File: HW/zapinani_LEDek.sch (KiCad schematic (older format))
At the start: 0 parts

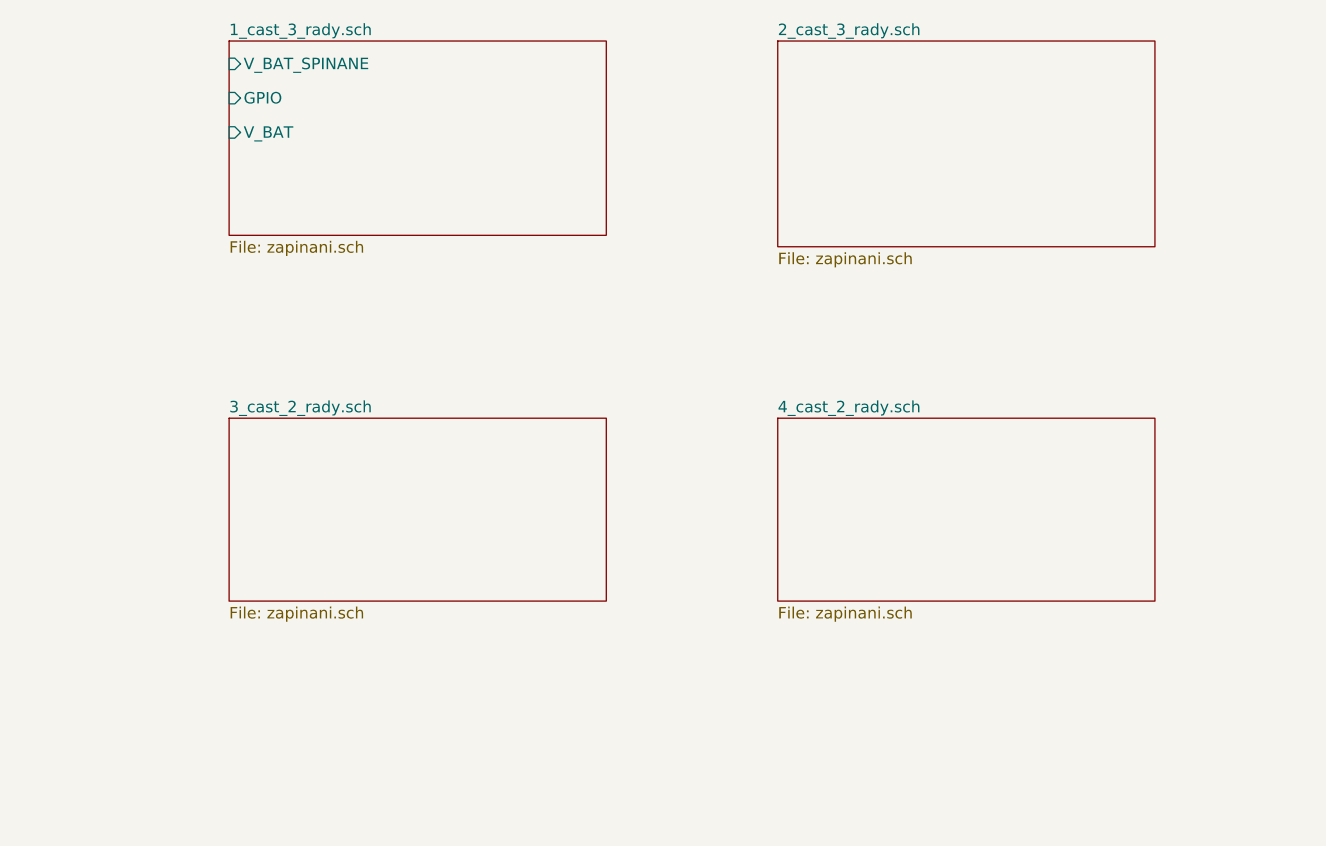
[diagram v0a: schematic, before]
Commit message: change structure of LEDs, add switching power supply of LEDs in parts
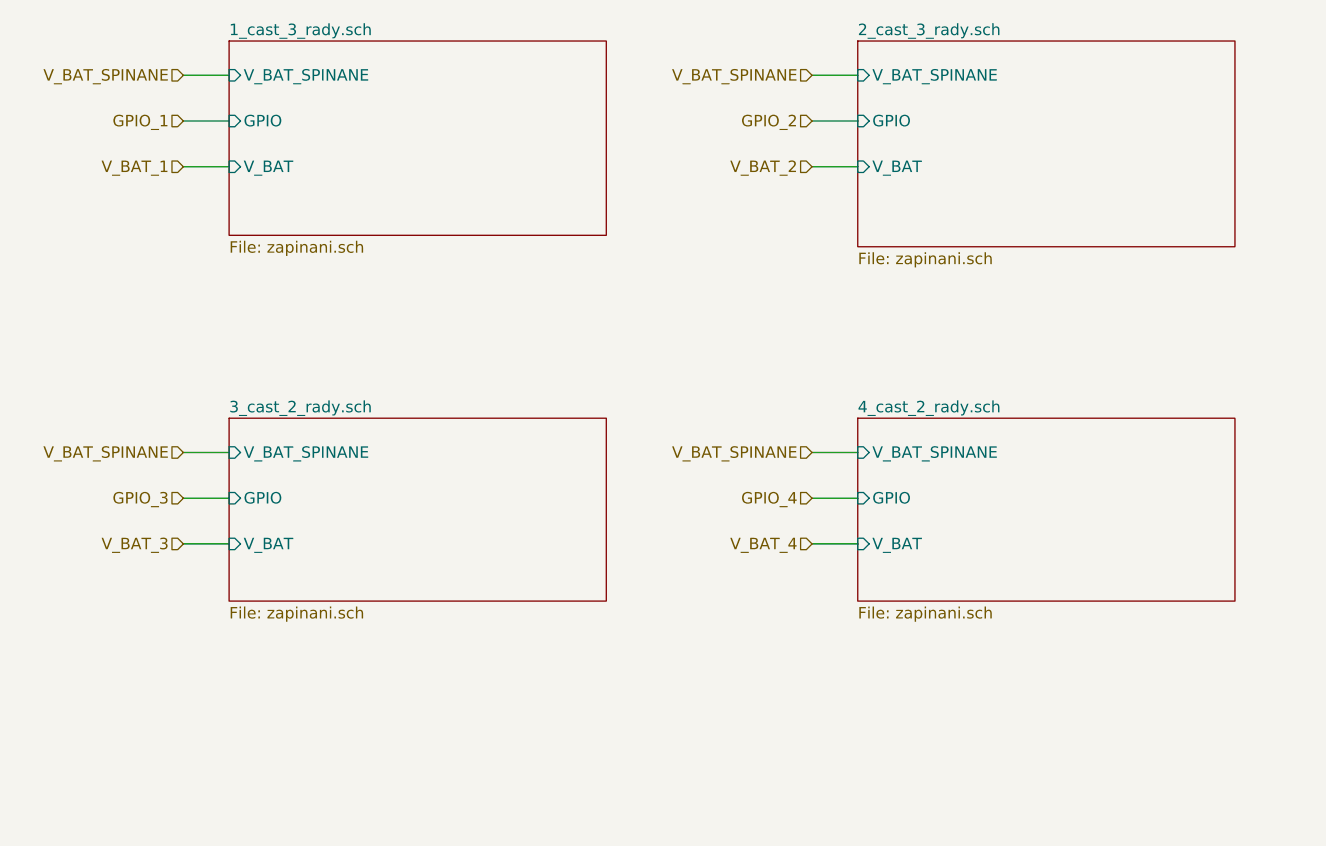
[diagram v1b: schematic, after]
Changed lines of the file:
@@
 $Descr A4 11693 8268
 encoding utf-8
-Sheet 18 22
+Sheet 18 42
 Title ""
 Date ""
@@
 F0 "1_cast_3_rady.sch" 50
 F1 "zapinani.sch" 50
-F2 "V_BAT_SPINANE" I L 1900 1150 50
-F3 "GPIO" I L 1900 1300 50
-F4 "V_BAT" I L 1900 1450 50
+F2 "V_BAT_SPINANE" I L 1900 1200 50
+F3 "GPIO" I L 1900 1400 50
+F4 "V_BAT" I L 1900 1600 50
 $EndSheet
 $Sheet
-S 4300 1050 1650 900
+S 4650 1050 1650 900
 U 5F7BCBA6
 F0 "2_cast_3_rady.sch" 50
 F1 "zapinani.sch" 50
+F2 "V_BAT_SPINANE" I L 4650 1200 50
+F3 "GPIO" I L 4650 1400 50
+F4 "V_BAT" I L 4650 1600 50
 $EndSheet
 $Sheet
@@
 F0 "3_cast_2_rady.sch" 50
 F1 "zapinani.sch" 50
+F2 "V_BAT_SPINANE" I L 1900 2850 50
+F3 "GPIO" I L 1900 3050 50
+F4 "V_BAT" I L 1900 3250 50
 $EndSheet
 $Sheet
-S 4300 2700 1650 800
+S 4650 2700 1650 800
 U 5F7BCC69
 F0 "4_cast_2_rady.sch" 50
 F1 "zapinani.sch" 50
+F2 "V_BAT_SPINANE" I L 4650 2850 50
+F3 "GPIO" I L 4650 3050 50
+F4 "V_BAT" I L 4650 3250 50
 $EndSheet
+Text HLabel 1700 1200 0    50   Input ~ 0
+V_BAT_SPINANE
+Text HLabel 4450 1200 0    50   Input ~ 0
+V_BAT_SPINANE
+Text HLabel 4450 2850 0    50   Input ~ 0
+V_BAT_SPINANE
+Text HLabel 1700 2850 0    50   Input ~ 0
+V_BAT_SPINANE
+Text HLabel 1700 1600 0    50   Input ~ 0
+V_BAT_1
+Text HLabel 4450 1600 0    50   Input ~ 0
+V_BAT_2
+Text HLabel 4450 3250 0    50   Input ~ 0
+V_BAT_4
+Text HLabel 1700 3250 0    50   Input ~ 0
+V_BAT_3
+Text HLabel 1700 1400 0    50   Input ~ 0
+GPIO_1
+Text HLabel 4450 1400 0    50   Input ~ 0
+GPIO_2
+Text HLabel 1700 3050 0    50   Input ~ 0
+GPIO_3
+Text HLabel 4450 3050 0    50   Input ~ 0
+GPIO_4
+Wire Wire Line
+	1700 1200 1900 1200
+Wire Wire Line
+	1900 1400 1700 1400
+Wire Wire Line
+	1700 1600 1900 1600
+Wire Wire Line
+	4450 1200 4650 1200
+Wire Wire Line
+	4650 1400 4450 1400
+Wire Wire Line
+	4450 1600 4650 1600
+Wire Wire Line
+	4650 2850 4450 2850
+Wire Wire Line
+	4450 3050 4650 3050
+Wire Wire Line
+	4650 3250 4450 3250
+Wire Wire Line
+	1700 2850 1900 2850
+Wire Wire Line
+	1900 3050 1700 3050
+Wire Wire Line
+	1700 3250 1900 3250
 $EndSCHEMATC

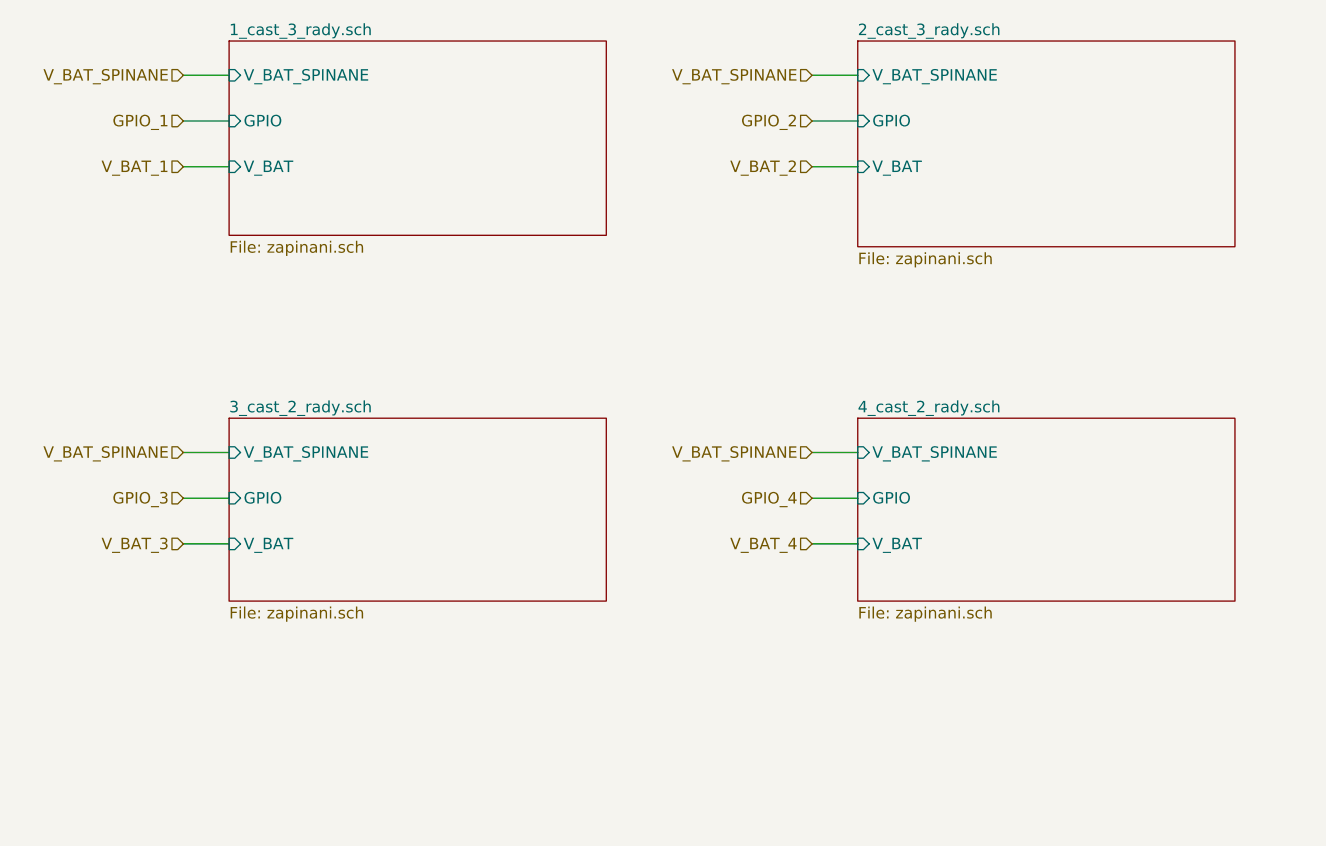
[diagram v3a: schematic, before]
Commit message: make smaller test version, start routing
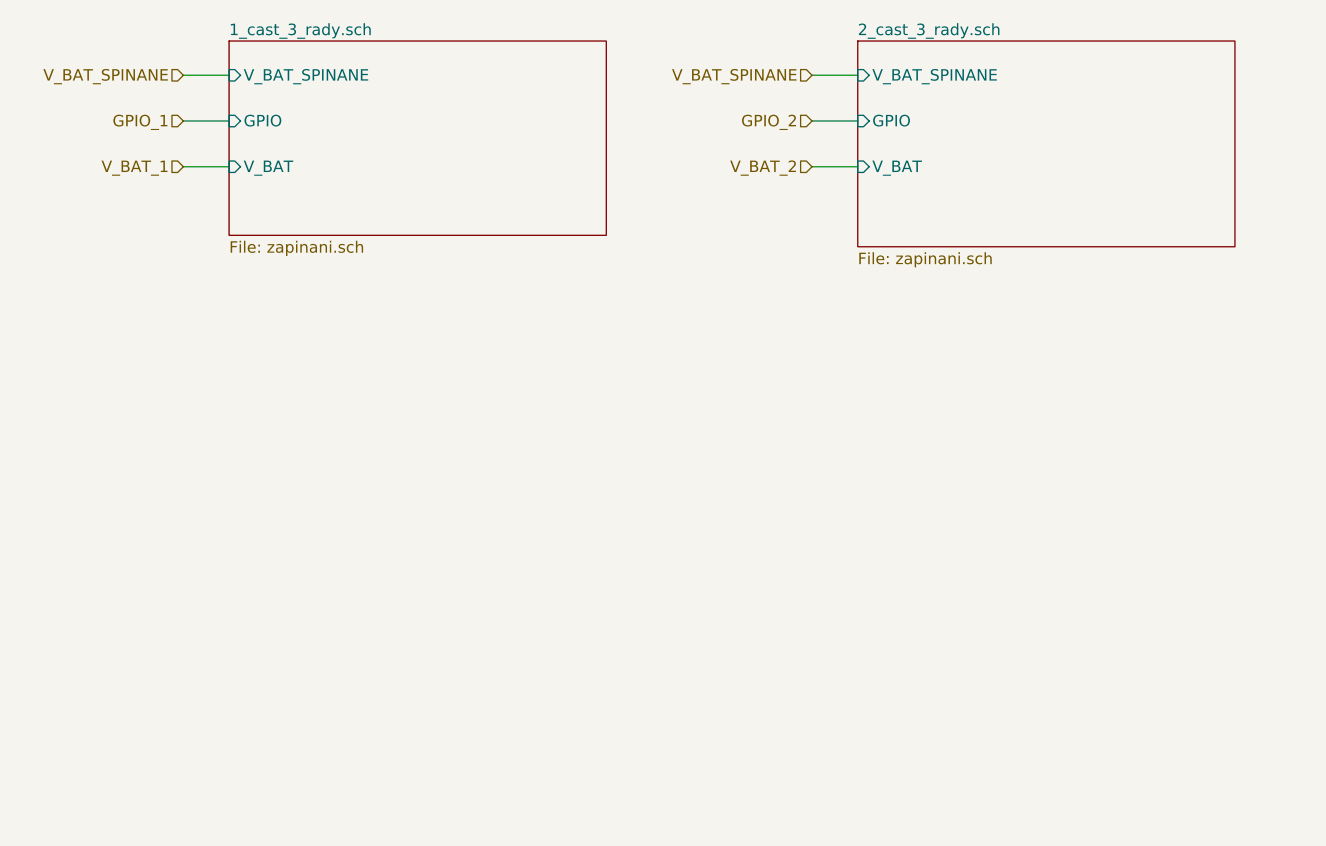
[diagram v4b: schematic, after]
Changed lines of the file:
@@
 $Descr A4 11693 8268
 encoding utf-8
-Sheet 16 44
+Sheet 16 34
 Title ""
 Date ""
@@
 F4 "V_BAT" I L 4650 1600 50
 $EndSheet
-$Sheet
-S 1900 2700 1650 800
-U 5F7BCC0A
-F0 "3_cast_2_rady.sch" 50
-F1 "zapinani.sch" 50
-F2 "V_BAT_SPINANE" I L 1900 2850 50
-F3 "GPIO" I L 1900 3050 50
-F4 "V_BAT" I L 1900 3250 50
-$EndSheet
-$Sheet
-S 4650 2700 1650 800
-U 5F7BCC69
-F0 "4_cast_2_rady.sch" 50
-F1 "zapinani.sch" 50
-F2 "V_BAT_SPINANE" I L 4650 2850 50
-F3 "GPIO" I L 4650 3050 50
-F4 "V_BAT" I L 4650 3250 50
-$EndSheet
 Text HLabel 1700 1200 0    50   Input ~ 0
 V_BAT_SPINANE
 Text HLabel 4450 1200 0    50   Input ~ 0
-V_BAT_SPINANE
-Text HLabel 4450 2850 0    50   Input ~ 0
-V_BAT_SPINANE
-Text HLabel 1700 2850 0    50   Input ~ 0
 V_BAT_SPINANE
 Text HLabel 1700 1600 0    50   Input ~ 0
@@
 Text HLabel 4450 1600 0    50   Input ~ 0
 V_BAT_2
-Text HLabel 4450 3250 0    50   Input ~ 0
-V_BAT_4
-Text HLabel 1700 3250 0    50   Input ~ 0
-V_BAT_3
 Text HLabel 1700 1400 0    50   Input ~ 0
 GPIO_1
 Text HLabel 4450 1400 0    50   Input ~ 0
 GPIO_2
-Text HLabel 1700 3050 0    50   Input ~ 0
-GPIO_3
-Text HLabel 4450 3050 0    50   Input ~ 0
-GPIO_4
 Wire Wire Line
 	1700 1200 1900 1200
@@
 Wire Wire Line
 	4450 1600 4650 1600
-Wire Wire Line
-	4650 2850 4450 2850
-Wire Wire Line
-	4450 3050 4650 3050
-Wire Wire Line
-	4650 3250 4450 3250
-Wire Wire Line
-	1700 2850 1900 2850
-Wire Wire Line
-	1900 3050 1700 3050
-Wire Wire Line
-	1700 3250 1900 3250
 $EndSCHEMATC

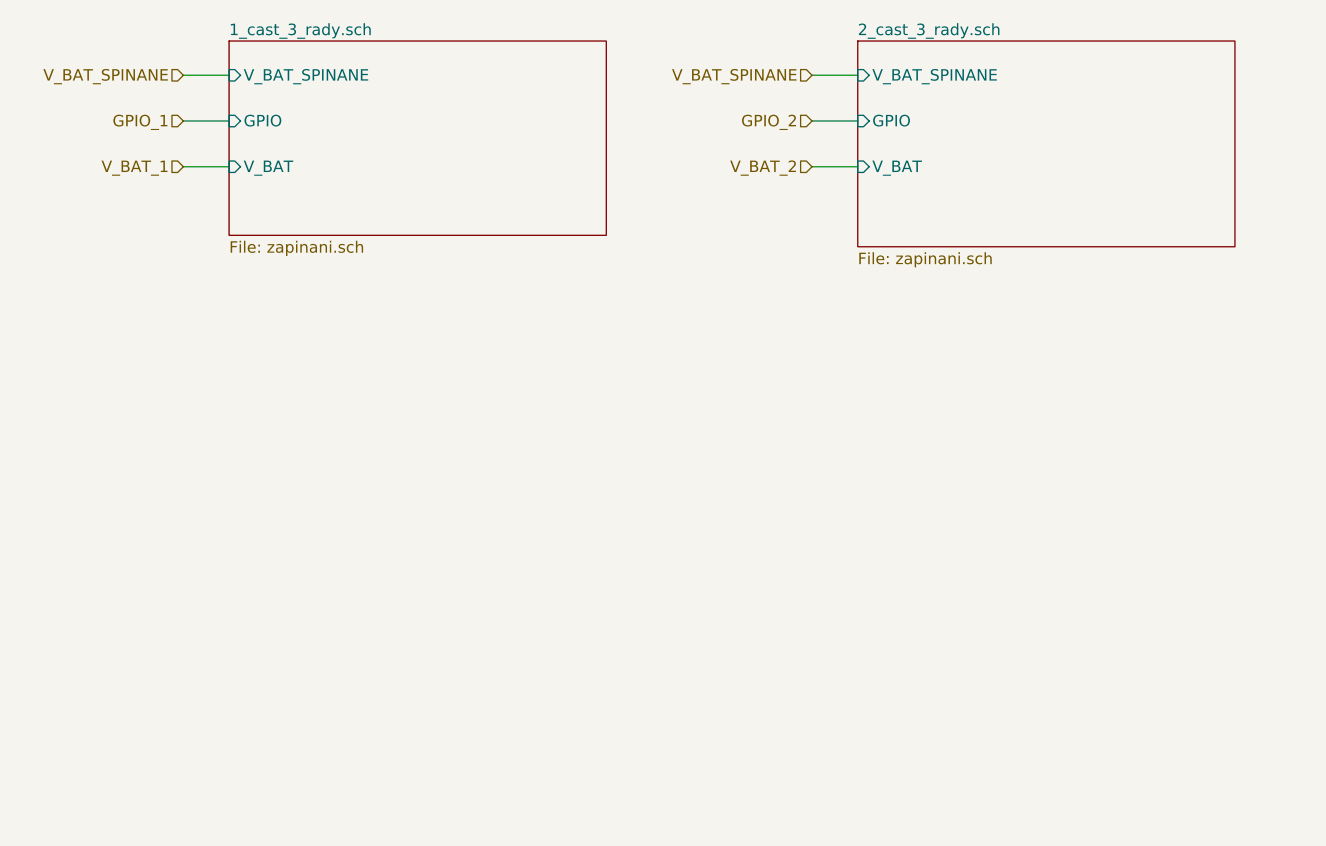
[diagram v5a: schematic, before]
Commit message: change structure of buttons, switching power
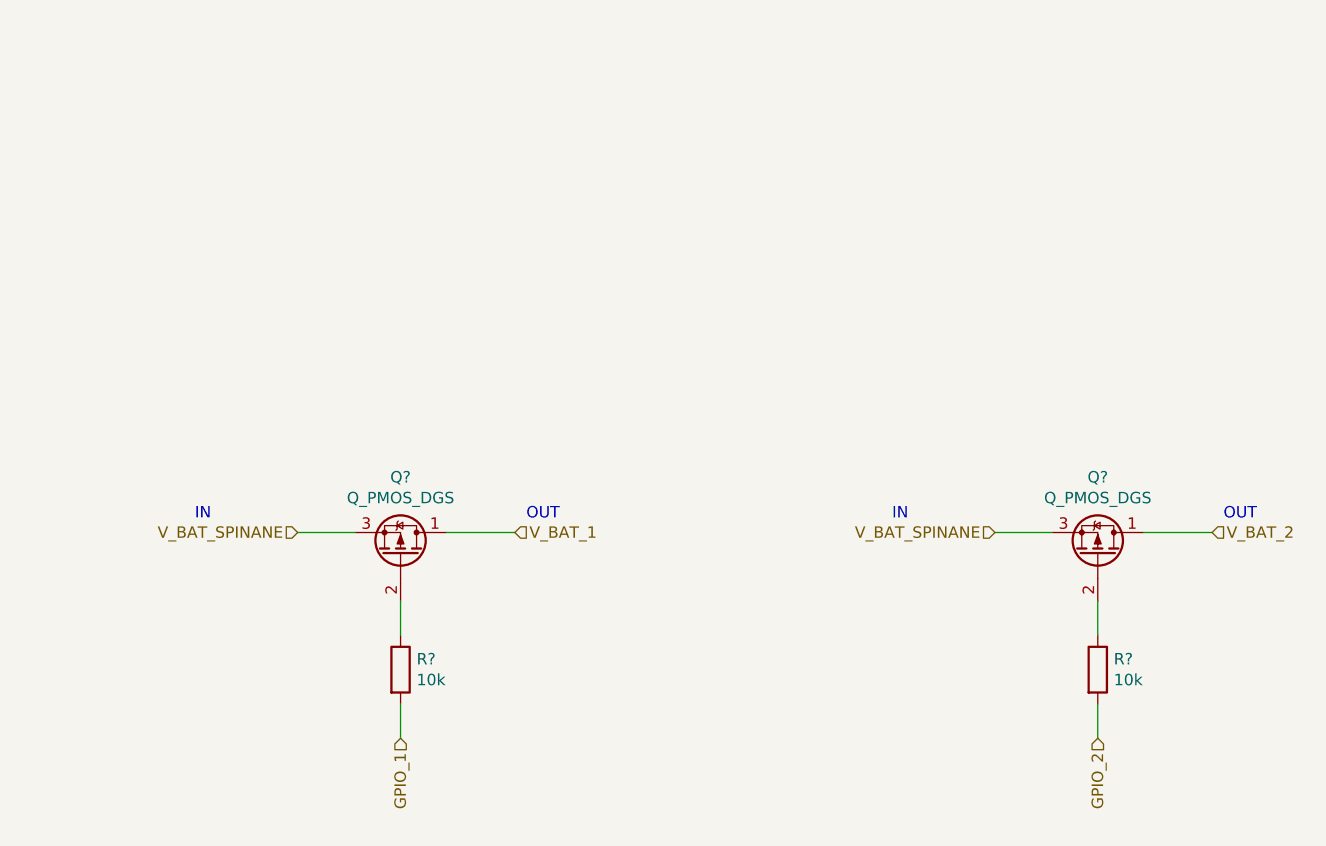
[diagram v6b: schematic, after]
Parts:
- added Q? (x2): Q_PMOS_DGS, Package_TO_SOT_SMD:SOT-23, symbol Device:Q_PMOS_DGS
- added R? (x2): 10k, Resistor_SMD:R_0402_1005Metric, symbol Device:R
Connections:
- net GPIO_1: now also R?.2
- net GPIO_2: now also R?.2
- net V_BAT_1: now also Q?.1 (D)
- net V_BAT_2: now also Q?.1 (D)
- net V_BAT_SPINANE: now also Q?.3 (S), Q?.3 (S)
- new net: Q?.2 (G), R?.1 (x2)
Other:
- note added: "IN\n"
- note added: "OUT\n"
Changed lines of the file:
@@
 $Descr A4 11693 8268
 encoding utf-8
-Sheet 32 34
+Sheet 21 21
 Title ""
 Date ""
@@
 Comment4 ""
 $EndDescr
-$Sheet
-S 1900 1050 1650 850
-U 5F7BCB45
-F0 "1_cast_3_rady.sch" 50
-F1 "zapinani.sch" 50
-F2 "V_BAT_SPINANE" I L 1900 1200 50
-F3 "GPIO" I L 1900 1400 50
-F4 "V_BAT" I L 1900 1600 50
-$EndSheet
-$Sheet
-S 4650 1050 1650 900
-U 5F7BCBA6
-F0 "2_cast_3_rady.sch" 50
-F1 "zapinani.sch" 50
-F2 "V_BAT_SPINANE" I L 4650 1200 50
-F3 "GPIO" I L 4650 1400 50
-F4 "V_BAT" I L 4650 1600 50
-$EndSheet
-Text HLabel 1700 1200 0    50   Input ~ 0
+Text HLabel 3150 3200 2    50   Input ~ 0
+V_BAT_1
+Text HLabel 2650 4100 3    50   Input ~ 0
+GPIO_1
+$Comp
+L Device:Q_PMOS_DGS Q?
+U 1 1 5F8EC64F
+P 2650 3300
+AR Path="/5F8EC64F" Ref="Q?"  Part="1"
+AR Path="/5F7BA54B/5F8EC64F" Ref="Q?"  Part="1"
+AR Path="/5F7BA54B/5F7BCB45/5F8EC64F" Ref="Q?"  Part="1"
+AR Path="/5F7BA54B/5F7BCBA6/5F8EC64F" Ref="Q?"  Part="1"
+AR Path="/5F7BA54B/5F7BCC0A/5F8EC64F" Ref="Q?"  Part="1"
+AR Path="/5F7BA54B/5F7BCC69/5F8EC64F" Ref="Q?"  Part="1"
+F 0 "Q?" V 2992 3300 50  0000 C CNN
+F 1 "Q_PMOS_DGS" V 2901 3300 50  0000 C CNN
+F 2 "Package_TO_SOT_SMD:SOT-23" H 2850 3400 50  0001 C CNN
+F 3 "~" H 2650 3300 50  0001 C CNN
+F 4 "C15127" H 2650 3300 50  0001 C CNN "LCSC"
+F 5 "0;0;180" H 2650 3300 50  0001 C CNN "JLCPCB_CORRECTION"
+	1    2650 3300
+	0    1    -1   0
+$EndComp
+$Comp
+L Device:R R?
+U 1 1 5F8EC656
+P 2650 3800
+AR Path="/5F8EC656" Ref="R?"  Part="1"
+AR Path="/5F7BA54B/5F8EC656" Ref="R?"  Part="1"
+AR Path="/5F7BA54B/5F7BCB45/5F8EC656" Ref="R?"  Part="1"
+AR Path="/5F7BA54B/5F7BCBA6/5F8EC656" Ref="R?"  Part="1"
+AR Path="/5F7BA54B/5F7BCC0A/5F8EC656" Ref="R?"  Part="1"
+AR Path="/5F7BA54B/5F7BCC69/5F8EC656" Ref="R?"  Part="1"
+F 0 "R?" H 2720 3846 50  0000 L CNN
+F 1 "10k" H 2720 3755 50  0000 L CNN
+F 2 "Resistor_SMD:R_0402_1005Metric" V 2580 3800 50  0001 C CNN
+F 3 "~" H 2650 3800 50  0001 C CNN
+F 4 "C25744" H 2650 3800 50  0001 C CNN "LCSC"
+	1    2650 3800
+	1    0    0    -1
+$EndComp
+Wire Wire Line
+	2200 3200 2450 3200
+Wire Wire Line
+	2850 3200 3150 3200
+Wire Wire Line
+	2650 3500 2650 3650
+Wire Wire Line
+	2650 3950 2650 4100
+Text HLabel 2200 3200 0    50   Input ~ 0
 V_BAT_SPINANE
-Text HLabel 4450 1200 0    50   Input ~ 0
+Text Notes 1750 3150 0    50   ~ 0
+IN\n
+Text Notes 3200 3150 0    50   ~ 0
+OUT\n
+Text HLabel 6200 3200 2    50   Input ~ 0
+V_BAT_2
+Text HLabel 5700 4100 3    50   Input ~ 0
+GPIO_2
+$Comp
+L Device:Q_PMOS_DGS Q?
+U 1 1 5F8ECA64
+P 5700 3300
+AR Path="/5F8ECA64" Ref="Q?"  Part="1"
+AR Path="/5F7BA54B/5F8ECA64" Ref="Q?"  Part="1"
+AR Path="/5F7BA54B/5F7BCB45/5F8ECA64" Ref="Q?"  Part="1"
+AR Path="/5F7BA54B/5F7BCBA6/5F8ECA64" Ref="Q?"  Part="1"
+AR Path="/5F7BA54B/5F7BCC0A/5F8ECA64" Ref="Q?"  Part="1"
+AR Path="/5F7BA54B/5F7BCC69/5F8ECA64" Ref="Q?"  Part="1"
+F 0 "Q?" V 6042 3300 50  0000 C CNN
+F 1 "Q_PMOS_DGS" V 5951 3300 50  0000 C CNN
+F 2 "Package_TO_SOT_SMD:SOT-23" H 5900 3400 50  0001 C CNN
+F 3 "~" H 5700 3300 50  0001 C CNN
+F 4 "C15127" H 5700 3300 50  0001 C CNN "LCSC"
+F 5 "0;0;180" H 5700 3300 50  0001 C CNN "JLCPCB_CORRECTION"
+	1    5700 3300
+	0    1    -1   0
+$EndComp
+$Comp
+L Device:R R?
+U 1 1 5F8ECA6B
+P 5700 3800
+AR Path="/5F8ECA6B" Ref="R?"  Part="1"
+AR Path="/5F7BA54B/5F8ECA6B" Ref="R?"  Part="1"
+AR Path="/5F7BA54B/5F7BCB45/5F8ECA6B" Ref="R?"  Part="1"
+AR Path="/5F7BA54B/5F7BCBA6/5F8ECA6B" Ref="R?"  Part="1"
+AR Path="/5F7BA54B/5F7BCC0A/5F8ECA6B" Ref="R?"  Part="1"
+AR Path="/5F7BA54B/5F7BCC69/5F8ECA6B" Ref="R?"  Part="1"
+F 0 "R?" H 5770 3846 50  0000 L CNN
+F 1 "10k" H 5770 3755 50  0000 L CNN
+F 2 "Resistor_SMD:R_0402_1005Metric" V 5630 3800 50  0001 C CNN
+F 3 "~" H 5700 3800 50  0001 C CNN
+F 4 "C25744" H 5700 3800 50  0001 C CNN "LCSC"
+	1    5700 3800
+	1    0    0    -1
+$EndComp
+Wire Wire Line
+	5250 3200 5500 3200
+Wire Wire Line
+	5900 3200 6200 3200
+Wire Wire Line
+	5700 3500 5700 3650
+Wire Wire Line
+	5700 3950 5700 4100
+Text HLabel 5250 3200 0    50   Input ~ 0
 V_BAT_SPINANE
-Text HLabel 1700 1600 0    50   Input ~ 0
-V_BAT_1
-Text HLabel 4450 1600 0    50   Input ~ 0
-V_BAT_2
-Text HLabel 1700 1400 0    50   Input ~ 0
-GPIO_1
-Text HLabel 4450 1400 0    50   Input ~ 0
-GPIO_2
-Wire Wire Line
-	1700 1200 1900 1200
-Wire Wire Line
-	1900 1400 1700 1400
-Wire Wire Line
-	1700 1600 1900 1600
-Wire Wire Line
-	4450 1200 4650 1200
-Wire Wire Line
-	4650 1400 4450 1400
-Wire Wire Line
-	4450 1600 4650 1600
+Text Notes 4800 3150 0    50   ~ 0
+IN\n
+Text Notes 6250 3150 0    50   ~ 0
+OUT\n
 $EndSCHEMATC
